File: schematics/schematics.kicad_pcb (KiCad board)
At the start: 2 copper layers, 83.3 x 76.1 mm, 27 parts, among them U1 4075

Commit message: More tests
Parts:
- removed 10, 11, 12, 13, 14 (x2), 5, 6, 7, 8, 9, ?: , 
- removed C1, C2, C3, C4, C5, C6: C_Small, Capacitor_SMD:C_1206_3216Metric
- removed U1: 4075, Package_SO:SOIC-14_3.9x8.7mm_P1.27mm
- added NAND1: SN74LS00NE4, CD74AC04E:DIP794W53P254L1930H508Q14N, B.Cu at (89.2, 67.6)
- added OR_1: CD4072BE, CD74AC04E:DIP794W53P254L1930H508Q14N, B.Cu at (48.7, 57.6)
- added XNOR1: CD4077BE, CD74AC04E:DIP794W53P254L1930H508Q14N, B.Cu at (48.8, 73.5)
- added ~{NMI}_SW1: SW_Push, Button_Switch_THT:SW_Tactile_SKHH_Angled, F.Cu at (102.2, 115.3)
- ADDR_1_LS1, ADDR_2_LS1, PICO_IN_LS1, PICO_OUT_LS1: footprint Package_SO:SO-20_5.3x12.6mm_P1.27mm -> SN74LVC245ANE4:DIP794W53P254L2540H508Q20N
- DATA_LS1: footprint Package_SO:SO-20_5.3x12.6mm_P1.27mm -> SN74LVC245ANE4:DIP794W53P254L2540H508Q20N; moved to B.Cu
- moved PICO_OUT_LS1 32.8 mm to (82.2, 117.6), turned to 90 degrees
- moved PICO_IN_LS1 28.2 mm to (54.0, 117.6), turned to 90 degrees
- moved DATA_LS1 27.4 mm to (89.2, 94.1)
- moved ADDR_2_LS1 14.4 mm to (69.7, 96.1)
- moved ADDR_1_LS1 10.6 mm to (69.2, 68.6)
- moved D1 9.69 mm to (103.2, 59.1), turned to 90 degrees
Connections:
- net ~{PI_EN} renamed ~{RP_EN}
- ADDR_1_LS1 pad 19: ~{OE} -> GND
- ADDR_2_LS1 pad 19: ~{OE} -> GND
- DATA_LS1 pad 1: ~{ZXRD} -> ~{RD}
- DATA_LS1 pad 12: D4 -> D6
- DATA_LS1 pad 13: D6 -> D5
- DATA_LS1 pad 14: D3 -> D4
- DATA_LS1 pad 15: D5 -> D3
- DATA_LS1 pad 19: ~{OE} -> ~{DATA_OE}
- DATA_LS1 pad 5: ZXD5 -> ZXD3
- DATA_LS1 pad 6: ZXD3 -> ZXD4
- DATA_LS1 pad 7: ZXD6 -> ZXD5
- DATA_LS1 pad 8: ZXD4 -> ZXD6
- PICO_IN_LS1 pad 14: unconnected-(PICO_IN_LS1-B4-Pad14) -> ~{CP/M}
- PICO_IN_LS1 pad 15: unconnected-(PICO_IN_LS1-B3-Pad15) -> ~{M1}
- PICO_IN_LS1 pad 19: ~{OE} -> GND
- PICO_IN_LS1 pad 5: unconnected-(PICO_IN_LS1-A3-Pad5) -> ~{ZXM1}
- PICO_IN_LS1 pad 6: unconnected-(PICO_IN_LS1-A4-Pad6) -> ~{ZXCP/M}
- PICO_OUT_LS1 pad 19: ~{OE} -> GND
- PICO_OUT_LS1 pad 3: ~{WAIT} -> ~{ZXWAIT}
- RP2040-PICO30 pad 32: SPARE_1 -> ~{M1}
- RP2040-PICO30 pad 34: SPARE_2 -> ~{CP/M}
- Z1 pad A14: unconnected-(Z1-~{NMI}-PadA14) -> ~{ZXNMI}
- Z1 pad A4: ~{ZX_CP/M} -> ~{ZXCP/M}
- Z1 pad B13: ~{ZXIORQGE} -> unconnected-(Z1-~{IORQGE}-PadB13)
- Z1 pad B15: ~{ZXROMCS2} -> unconnected-(Z1-~{ROMCS2}-PadB15)
- Z1 pad B25: ~{ZX_ROMCS} -> ~{ZXROMCS}
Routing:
- net ~{ZXPI_EN}: track 0.00 -> 186.7 mm, vias 0 -> 1
- net ~{ZXM1}: track 0.00 -> 138.5 mm, vias 0 -> 1
- net ~{ZXNMI}: track 0.00 -> 127.1 mm, vias 0 -> 2
- net ZXD0: track 0.00 -> 115.9 mm, vias 0 -> 2
- net ~{ZXCP/M}: track 0.00 -> 105.4 mm, vias 0 -> 1
- net ~{ZXMREQ}: track 0.00 -> 100.4 mm
- net +3V3: track 135.3 -> 41.4 mm, vias 6 -> 15
- net ~{ZXIORQ}: track 0.00 -> 91.4 mm, vias 0 -> 1
- net ZXA13: track 0.00 -> 89.4 mm, vias 0 -> 1
- net ~{ZXRD}: track 0.00 -> 85.4 mm, vias 0 -> 3
- net ZXA12: track 0.00 -> 84.6 mm, vias 0 -> 1
- net ZXD7: track 0.00 -> 84.4 mm
- net ZXD1: track 0.00 -> 80.2 mm, vias 0 -> 2
- net ~{CP/M}: track 0.00 -> 80.0 mm, vias 0 -> 2
- net ~{M1}: track 0.00 -> 79.1 mm, vias 0 -> 2
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- added copper zone on F.Cu, net +3V3
- removed copper zone on F.Cu, net GND
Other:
- board text added: "IFp v0.1"
- board text removed: "GPIO27"
- board text removed: "GPIO28"
- board text removed: "github.com/derekfountain/zx-spectrum-pico-rom v1.2"

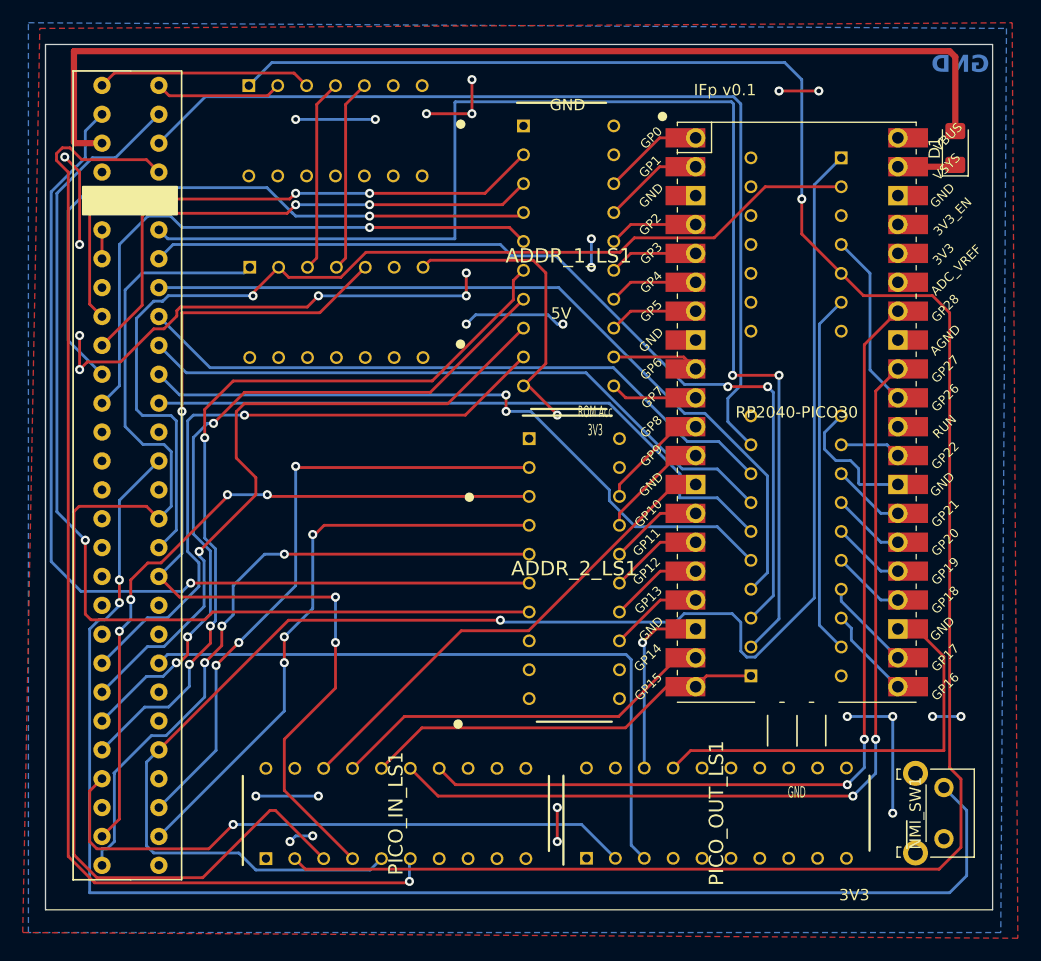
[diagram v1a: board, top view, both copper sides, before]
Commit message: Switched to olimex pico2 xxl
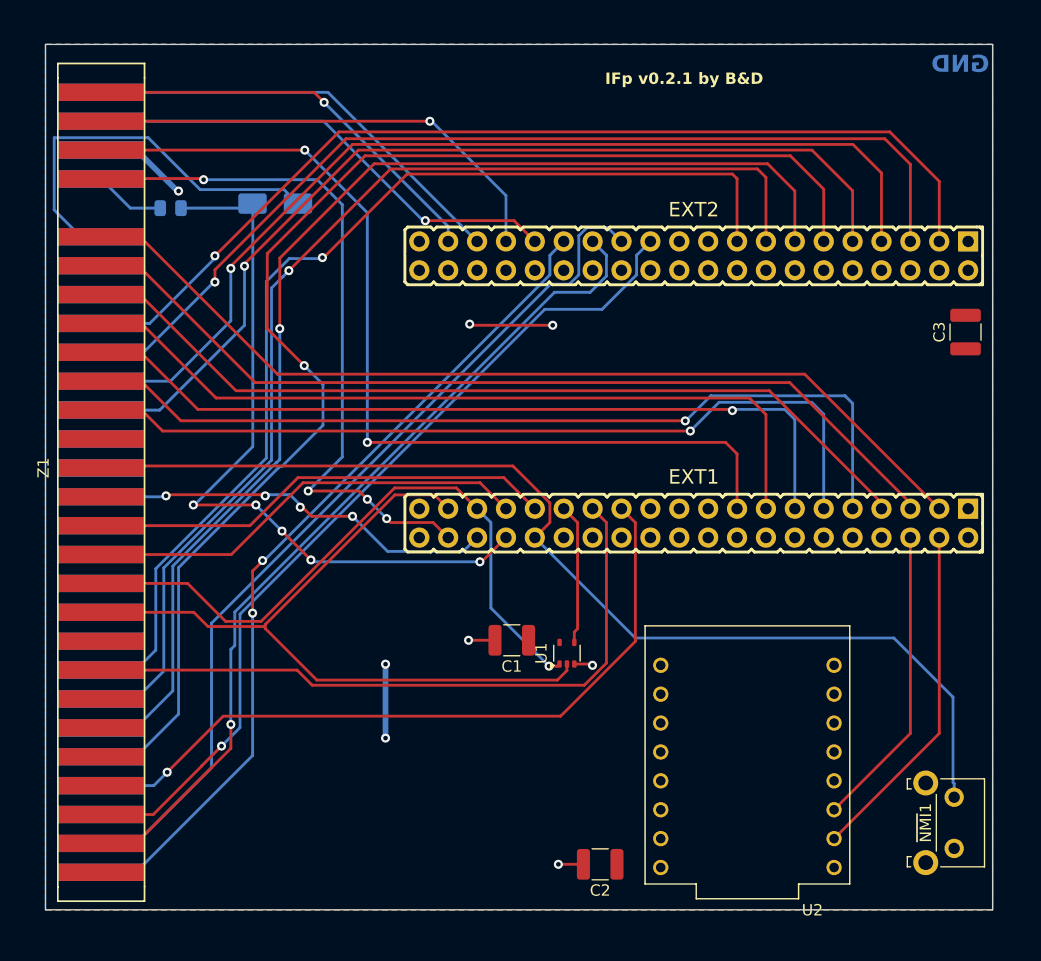
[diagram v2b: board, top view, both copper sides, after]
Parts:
- removed ADDR_1_LS1, ADDR_2_LS1, DATA_LS1, PICO_IN_LS1, PICO_OUT_LS1: 74LS245, SN74LVC245ANE4:DIP794W53P254L2540H508Q20N
- removed NAND1: SN74LS00NE4, CD74AC04E:DIP794W53P254L1930H508Q14N
- removed OR_1: CD4072BE, CD74AC04E:DIP794W53P254L1930H508Q14N
- removed RP2040-PICO30: RP2040-PICO30, pico-foot:RPi_Pico_SMD_TH
- removed XNOR1: CD4077BE, CD74AC04E:DIP794W53P254L1930H508Q14N
- removed ~{NMI}_SW1: SW_Push, Button_Switch_THT:SW_Tactile_SKHH_Angled
- added C1: 0.1uF, Capacitor_SMD:C_1210_3225Metric, F.Cu at (64.2, 102.4)
- added C2: 0.1uF, Capacitor_SMD:C_1210_3225Metric, F.Cu at (72.0, 122.1)
- added C3: 0.1uF, Capacitor_SMD:C_1210_3225Metric, F.Cu at (104.1, 75.3)
- added EXT1: NA(HN2x20), OLIMEX_Connectors-FP:HN2x20, F.Cu at (80.2, 92.1)
- added EXT2: NA(HN2x20), OLIMEX_Connectors-FP:HN2x20, F.Cu at (80.2, 68.6)
- added R1: 1K, Resistor_SMD:R_0805_2012Metric, B.Cu at (34.2, 64.4)
- added U1: 74LVC1G86, Package_TO_SOT_SMD:SOT-353_SC-70-5, F.Cu at (69.0, 103.5)
- added U2: ESP32-C3_SUPERMINI_TH, ESP32-C_SUPERMINI:MODULE_ESP32-C3_SUPERMINI_TH, F.Cu at (84.9, 112.5)
- added ~{NMI}1: ~{NMI}, Button_Switch_THT:SW_Tactile_SKHH_Angled, F.Cu at (103.1, 116.2)
- D1: value D_Schottky -> Z1SMAxxx; footprint Diode_SMD:D_1206_3216Metric_Pad1.42x1.75mm_HandSolder -> Diode_SMD:D_SMA; moved to B.Cu
- Z1: footprint zxbus:ZX_Bus_Pin_Header -> zxbus:ZX_Bus_Edge_Connector
- moved D1 60.0 mm to (43.4, 64.0), turned to 0 degrees
- moved Z1 0.66 mm to (28.1, 87.2)
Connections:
- D1 pad 1: Net-(D1-K) -> /J_HC_CPM
- D1 pad 2: +5V -> GND
- Z1 pad A19: unconnected-(Z1-~{WR}-PadA19) -> ~{ZXWR}
- Z1 pad A24: ~{ZXM1} -> unconnected-(Z1-~{M1}-PadA24)
- Z1 pad A4: ~{ZXCP/M} -> ZXROMCS1
- Z1 pad B15: unconnected-(Z1-~{ROMCS2}-PadB15) -> ZXROMCS2
- Z1 pad B25: ~{ZXROMCS} -> ZXROMCS
- Z1 pad B4: unconnected-(Z1-+9V-PadB4) -> HC_CPM
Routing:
- net ~{ZXPI_EN}: track 186.7 -> 0.00 mm, vias 1 -> 0
- net ~{ZXM1}: track 138.5 -> 0.00 mm, vias 1 -> 0
- net ~{ZXCP/M}: track 105.4 -> 0.00 mm, vias 1 -> 0
- net +5V: track 94.7 -> 11.7 mm, vias 0 -> 3
- net ~{CP/M}: track 80.0 -> 0.00 mm, vias 2 -> 0
- net ~{M1}: track 79.1 -> 0.00 mm, vias 2 -> 0
- net ~{ZXWR}: track 0.00 -> 65.6 mm
- net /J_HC_CPM: track 0.00 -> 65.1 mm, vias 0 -> 5
- net ZXROMCS: track 0.00 -> 64.4 mm, vias 0 -> 1
- net ZXROMCS1: track 0.00 -> 62.6 mm, vias 0 -> 4
- net ~{ZXMREQ}: track 100.4 -> 41.0 mm
- net ~{ZXROMCS}: track 54.6 -> 0.00 mm, vias 1 -> 0
- net ~{ZXIORQ}: track 91.4 -> 39.1 mm, vias 1 -> 0
- net ZXA13: track 89.4 -> 42.3 mm
- net ZXA4: track 70.1 -> 114.5 mm, vias 3 -> 1
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- added copper zone on F.Cu, net +5V
- removed copper zone on F.Cu, net +3V3
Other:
- board text added: "IFp v0.2.1 by B&D"
- board text removed: "3V3"
- board text removed: "5V"
- board text removed: "IFp v0.1"
- board text removed: "ROM Acc 3V3"

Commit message: Fix BogDan is an idiot wrong line assignment
Fixes: #1, #3
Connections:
- EXT1 pad 32: ~{ZXNMI} -> /GPIO12\SPI1_RX\SD_DAT0
- EXT1 pad 8: /GPIO2\I2C1_SDA -> ~{ZXNMI}
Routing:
- net ~{ZXNMI}: track 95.9 -> 97.5 mm
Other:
- board text added: "IFp v0.3.0 by B&D"
- board text removed: "IFp v0.2.1 by B&D"
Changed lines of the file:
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@@
 	(net 54 "/GPIO6\\SPI0_SCK(SCK)")
 	(net 55 "/GPIO3\\I2C1_SCL")
-	(net 56 "/GPIO2\\I2C1_SDA")
+	(net 56 "/GPIO12\\SPI1_RX\\SD_DAT0")
 	(net 57 "/GPIO4\\SPI0_RX(MISO)")
 	(net 58 "/GPIO11\\SPI1_TX\\SD_CMD")
@@
 			(layers "*.Cu" "*.Mask")
 			(remove_unused_layers no)
-			(net 56 "/GPIO2\\I2C1_SDA")
+			(net 48 "~{ZXNMI}")
 			(pinfunction "8")
 			(pintype "passive")
@@
 			(layers "*.Cu" "*.Mask")
 			(remove_unused_layers no)
-			(net 48 "~{ZXNMI}")
+			(net 56 "/GPIO12\\SPI1_RX\\SD_DAT0")
 			(pinfunction "32")
 			(pintype "passive")
@@
 		)
 	)
-	(gr_text "IFp v0.2.1 by B&D"
+	(gr_text "IFp v0.3.0 by B&D"
 		(at 72.38 53.57 0)
 		(layer "F.SilkS" knockout)
@@
 	)
 	(segment
-		(start 64.28227 87.044)
-		(end 67.535 90.29673)
+		(start 28.246 87.044)
+		(end 79.644 87.044)
 		(width 0.25)
 		(layer "F.Cu")
@@
 	)
 	(segment
-		(start 28.08 87.21)
-		(end 28.246 87.044)
+		(start 83.42173 92.06)
+		(end 95.41 92.06)
 		(width 0.25)
 		(layer "F.Cu")
@@
 	)
 	(segment
-		(start 67.535 92.015)
-		(end 66.21 93.34)
+		(start 82.68 91.31827)
+		(end 83.42173 92.06)
 		(width 0.25)
 		(layer "F.Cu")
@@
 	)
 	(segment
-		(start 28.246 87.044)
-		(end 64.28227 87.044)
+		(start 82.68 90.08)
+		(end 82.68 91.31827)
 		(width 0.25)
 		(layer "F.Cu")
@@
 	)
 	(segment
-		(start 67.535 90.29673)
-		(end 67.535 92.015)
+		(start 95.41 92.06)
+		(end 96.69 93.34)
 		(width 0.25)
 		(layer "F.Cu")
@@
 	)
 	(segment
-		(start 97.78 102.17)
-		(end 102.98 107.37)
+		(start 28.08 87.21)
+		(end 28.246 87.044)
 		(width 0.25)
-		(layer "B.Cu")
+		(layer "F.Cu")
 		(net 48)
 	)
 	(segment
-		(start 66.21 93.34)
-		(end 75.04 102.17)
+		(start 79.644 87.044)
+		(end 82.68 90.08)
+		(width 0.25)
+		(layer "F.Cu")
+		(net 48)
+	)
+	(segment
+		(start 102.98 114.867919)
+		(end 103.08 114.967919)
 		(width 0.25)
 		(layer "B.Cu")
@@
 	)
 	(segment
-		(start 102.98 107.37)
-		(end 102.98 114.867919)
+		(start 103.08 114.967919)
+		(end 103.08 116.17)
 		(width 0.25)
 		(layer "B.Cu")
@@
 	)
 	(segment
-		(start 75.04 102.17)
-		(end 97.78 102.17)
+		(start 96.69 93.34)
+		(end 96.69 101.08)
 		(width 0.25)
 		(layer "B.Cu")
@@
 	)
 	(segment
-		(start 102.98 114.867919)
-		(end 103.08 114.967919)
+		(start 96.69 101.08)
+		(end 102.98 107.37)
 		(width 0.25)
 		(layer "B.Cu")
@@
 	)
 	(segment
-		(start 103.08 114.967919)
-		(end 103.08 116.17)
+		(start 102.98 107.37)
+		(end 102.98 114.867919)
 		(width 0.25)
 		(layer "B.Cu")

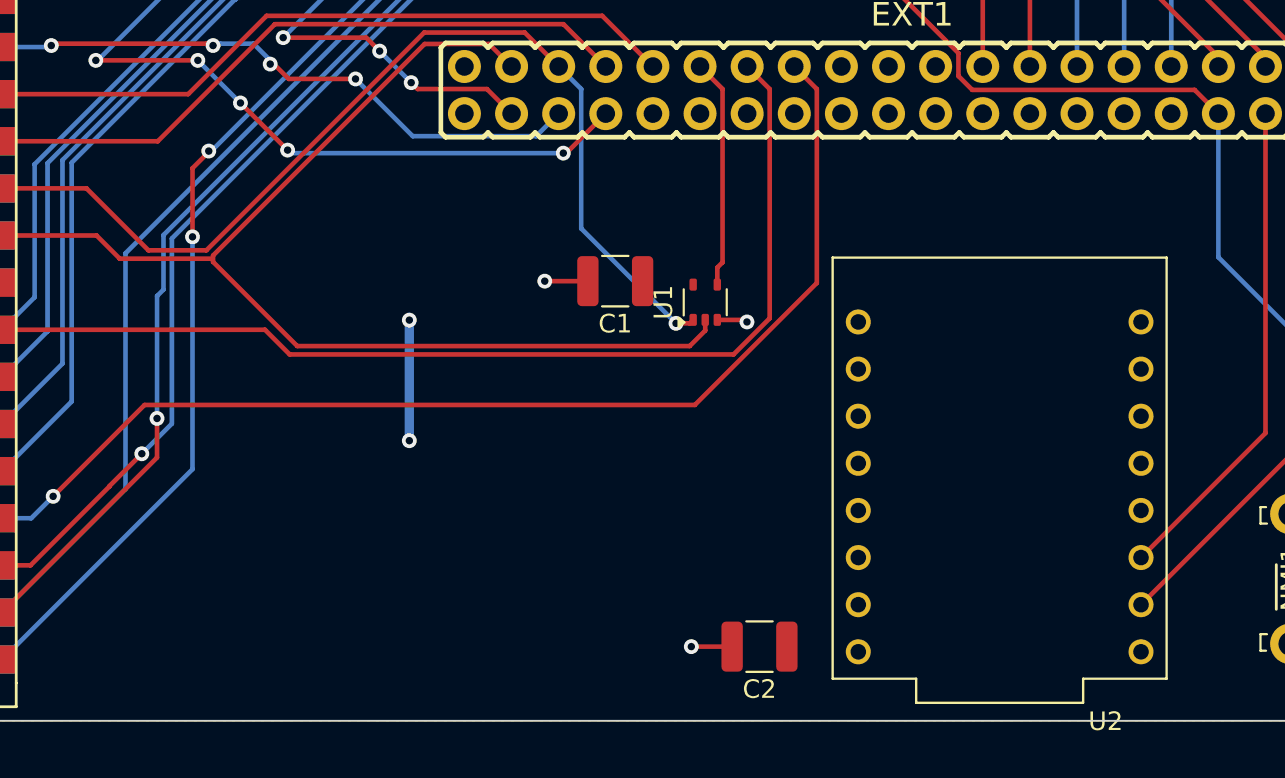
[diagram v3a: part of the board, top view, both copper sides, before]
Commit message: Add kempston joystick
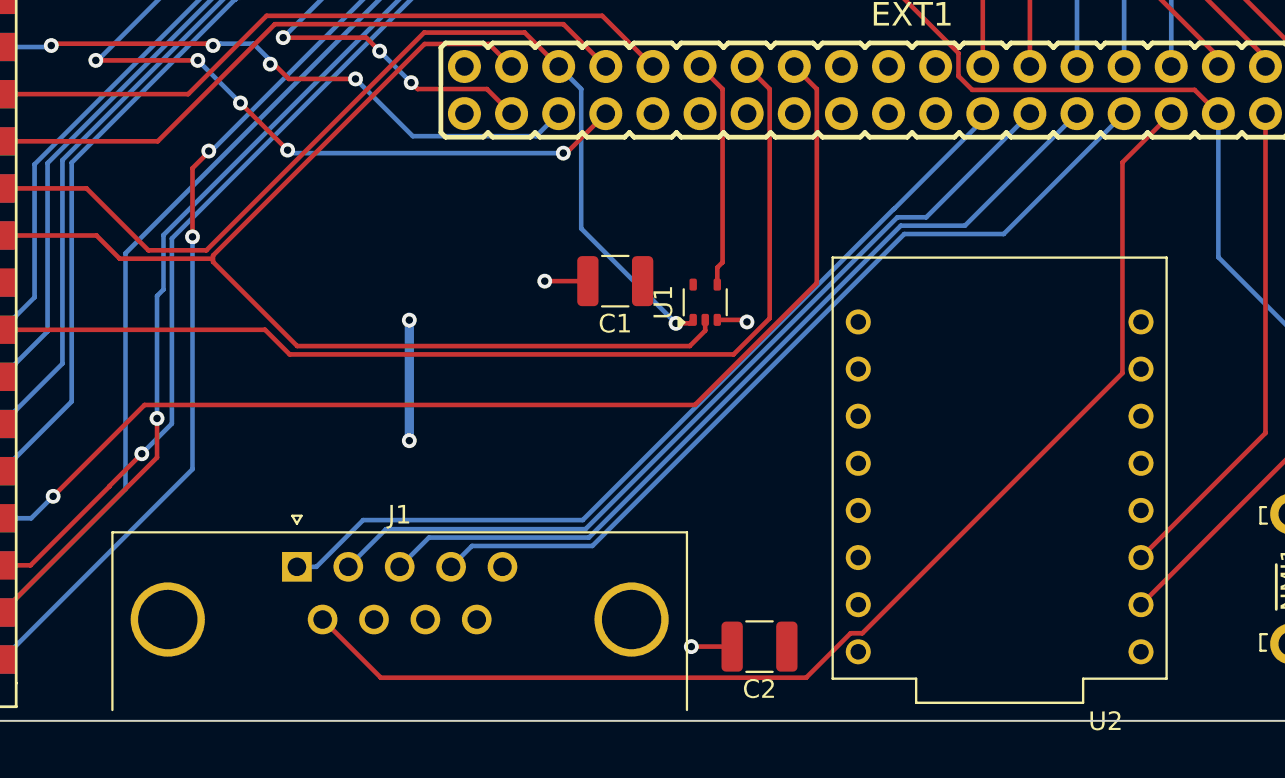
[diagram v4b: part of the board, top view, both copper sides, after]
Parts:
- added J1: DE9_Pins_MountingHoles, Connector_Dsub:DSUB-9_Pins_Horizontal_P2.77x2.84mm_EdgePinOffset4.94mm_Housed_MountingHolesOffset4.94mm, F.Cu at (47.0, 117.8)
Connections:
- EXT1 pad 10: /GPIO3\I2C1_SCL -> /FIRE
- EXT1 pad 12: /GPIO4\SPI0_RX(MISO) -> /RIGHT
- EXT1 pad 14: /GPIO5\SPI0_CSn(CS#) -> /LEFT
- EXT1 pad 16: /GPIO6\SPI0_SCK(SCK) -> /DOWN
- EXT1 pad 18: /GPIO7\SPI0_TX(MOSI) -> /UP
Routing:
- net /FIRE: track 0.00 -> 66.3 mm
- net /UP: track 0.00 -> 47.3 mm
- net /DOWN: track 0.00 -> 46.9 mm
- net /LEFT: track 0.00 -> 46.6 mm
- net /RIGHT: track 0.00 -> 46.4 mm
